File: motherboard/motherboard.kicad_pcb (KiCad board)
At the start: 2 copper layers, 79.8 x 53.3 mm, 54 parts, among them J1 locked, J2 PROGRAM, J3 Battery / Pitot/ Orientation, J4 c02 censor, J5 shaftencorder, J6 USB_C_Receptacle_USB2.0, J7 SparLoad, J8 lidar, J9 Control Board, Q1 2N7002K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

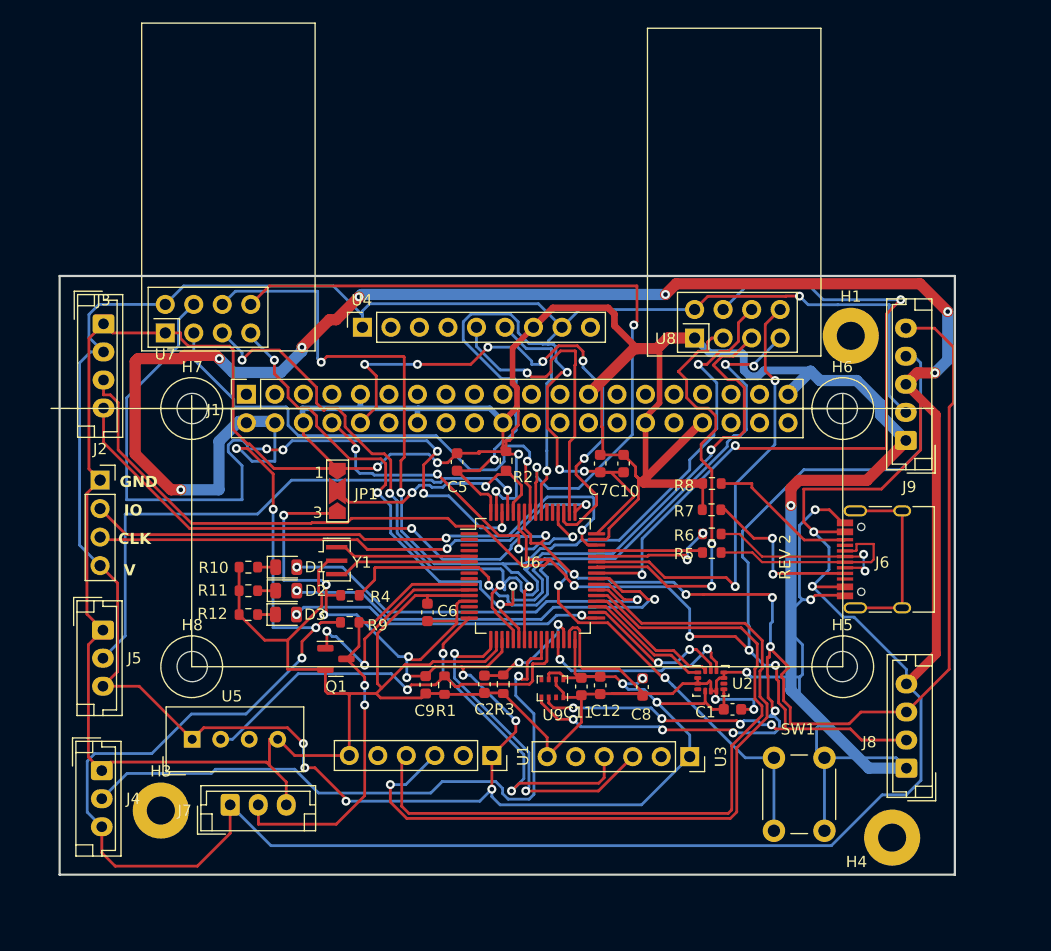
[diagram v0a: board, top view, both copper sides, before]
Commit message: PCB Rev2 Layout
PCB layout revised with ground and power pours, differential routing for USB, fixes for USB and programming pins. Passes DRC.
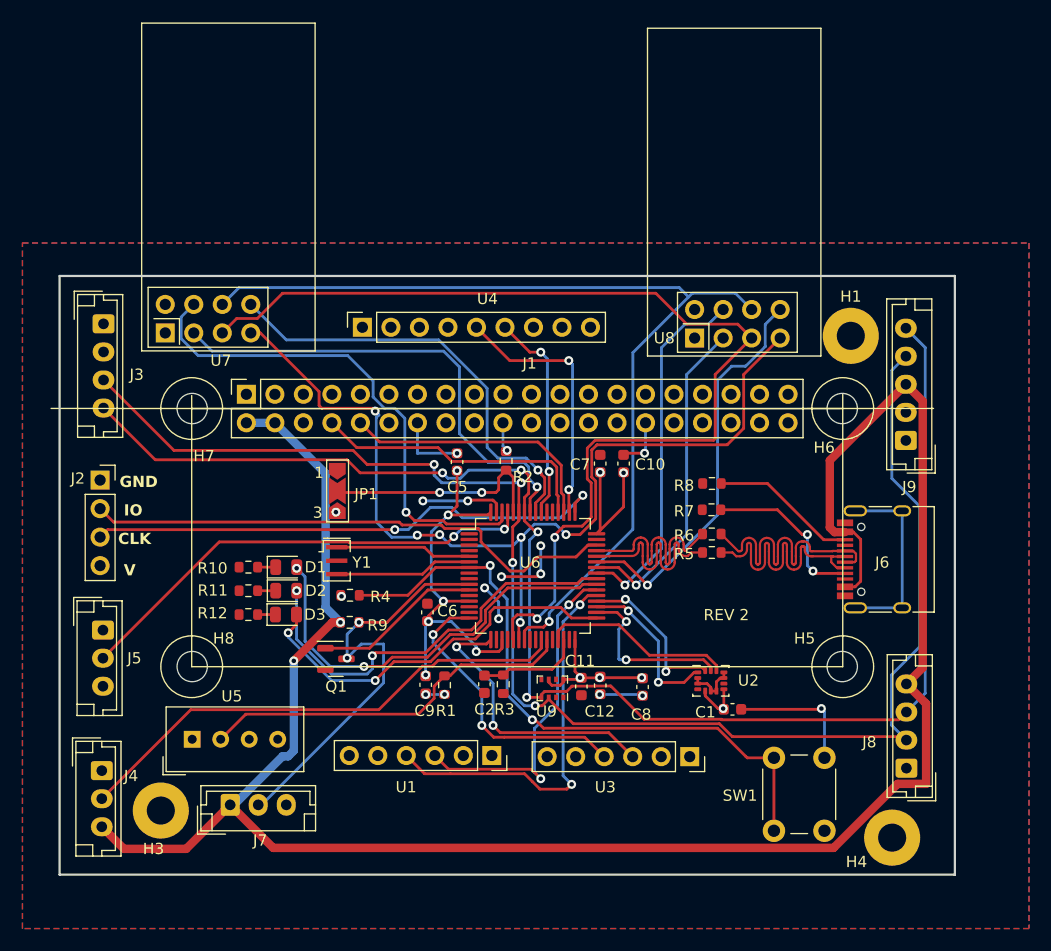
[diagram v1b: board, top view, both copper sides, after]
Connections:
- net Net-(D1-A) renamed /LED1
- net Net-(D2-A) renamed /LED2
- net Net-(D3-A) renamed /LED3
- R5 pad 1: /USB_{D+} -> /USB-
- R5 pad 2: /D+ -> /D-
- R6 pad 1: /USB_{D-} -> /USB+
- R6 pad 2: /D- -> /D+
- U6 pad 44: /USB_{D-} -> /USB-
- U6 pad 45: /USB_{D+} -> /USB+
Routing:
- net GND: track 500.0 -> 52.7 mm, vias 10 -> 15
- net +3.3V: track 352.2 -> 65.7 mm, vias 19 -> 14
- net +5V: track 346.3 -> 185.5 mm, vias 13 -> 2
- net /USART6_{RX}: track 71.7 -> 30.3 mm, vias 1 -> 2
- net /I2C_{SCK}: track 170.0 -> 133.5 mm, vias 10 -> 4
- net /USART6_{TX}: track 66.8 -> 35.0 mm, vias 0 -> 2
- net /TELE_{CS}-E: track 63.8 -> 32.4 mm, vias 3 -> 1
- net /I2C_{SDA}: track 161.6 -> 135.4 mm, vias 8 -> 4
- net /TELE_{IRQ}-int: track 64.3 -> 39.1 mm, vias 2 -> 1
- net /USART3_{TX}: track 49.0 -> 23.7 mm, vias 6 -> 0
- net /TELE_{CS}-int: track 69.6 -> 45.5 mm, vias 5 -> 1
- net /USB+: track 0.00 -> 19.8 mm
- net /USB-: track 0.00 -> 19.3 mm
- net /CO_{2}: track 58.8 -> 45.5 mm, vias 1 -> 0
- net /USB_{D-}: track 11.5 -> 0.00 mm, vias 2 -> 0
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- added copper zone on B.Cu, net +3.3V
- added copper zone on F.Cu, net GND
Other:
- board text added: "Ethan Todd"

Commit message: Touched up layout
Updated title block and made revision label used title block value
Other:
- board text added: "REV ${REVISION}"
- board text removed: "REV 2"
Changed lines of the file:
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@@
   (paper "A4")
   (title_block
-    (rev "REV2")
+    (title "Falcon Motherboard")
+    (date "2024-02-15")
+    (rev "2")
+    (company "HPVDT")
   )
   (layers
@@
     (effects (font (size 1 1) (thickness 0.25) bold) (justify left bottom))
   )
-  (gr_text "REV 2" (at 129.5 91.75) (layer "F.SilkS" knockout)
+  (gr_text "REV ${REVISION}" (at 129.5 91.75) (layer "F.SilkS" knockout)
     (effects (font (size 1 1) (thickness 0.15)) (justify left bottom))
   )

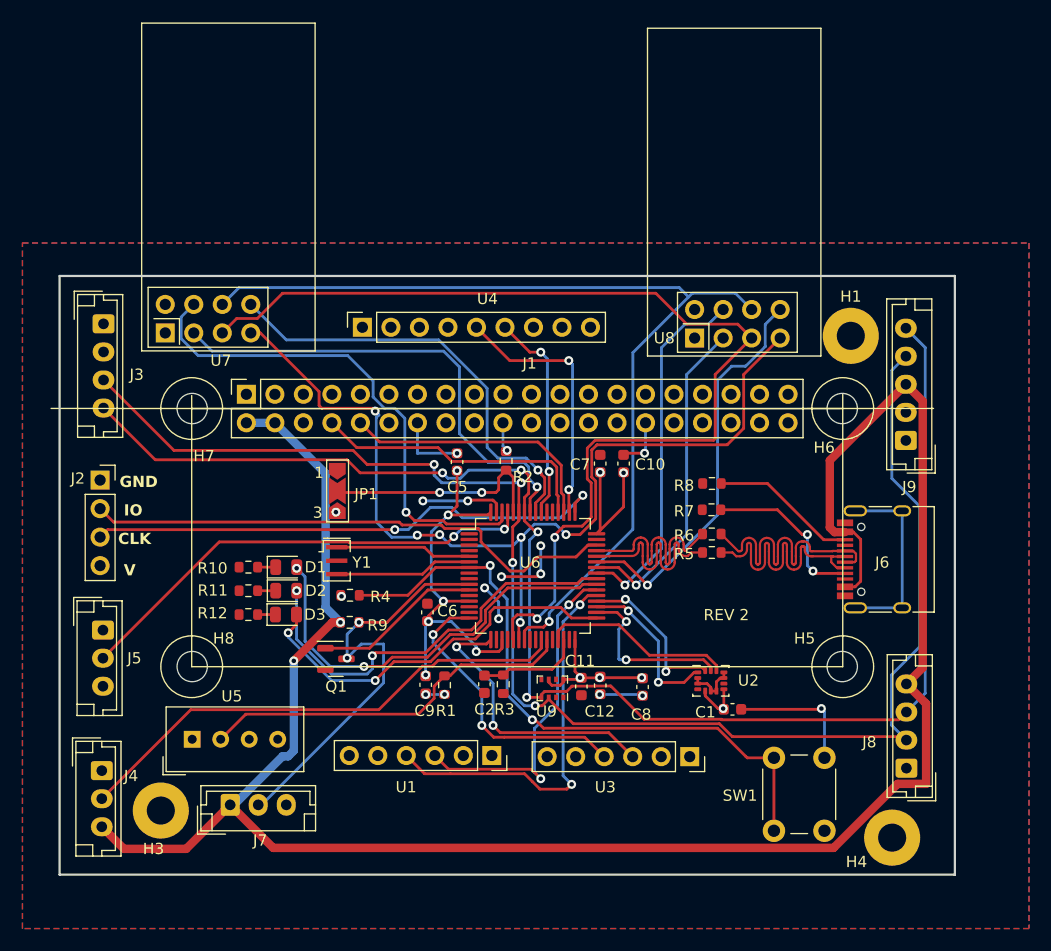
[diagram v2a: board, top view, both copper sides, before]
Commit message: Added extra LEDs, replaced Voltage reg., added redundant SW, reviewed USB placement
Added many new features
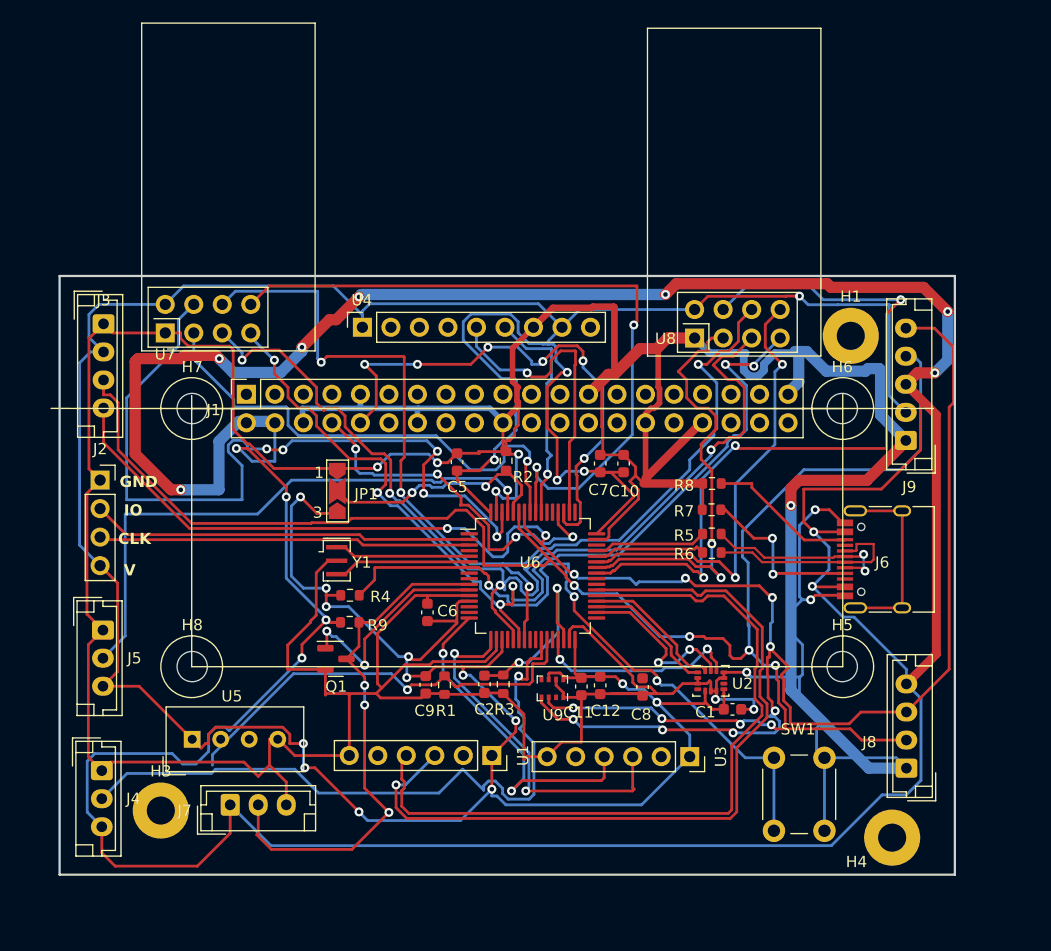
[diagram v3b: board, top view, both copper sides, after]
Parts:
- removed D1, D2, D3: LED, LED_SMD:LED_0805_2012Metric
- removed R10, R11, R12: 130R, Resistor_SMD:R_0603_1608Metric
- renumbered R6 to R5, R5 to R6
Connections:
- net /USB+ renamed /USB_{D-}
- net /USB- renamed /USB_{D+}
- R5 pad 2: /D+ -> /D-
- R6 pad 2: /D- -> /D+
- U6 pad 2: unconnected-(U6-PC13-Pad2) -> /SWDIO
- U6 pad 3: unconnected-(U6-PC14-Pad3) -> /SWCLK
- U6 pad 33: /LED3 -> unconnected-(U6-PB12-Pad33)
- U6 pad 39: /LED1 -> unconnected-(U6-PC8-Pad39)
- U6 pad 40: /LED2 -> unconnected-(U6-PC9-Pad40)
- U6 pad 46: /SWDIO -> unconnected-(U6-PA13-Pad46)
- U6 pad 49: /SWCLK -> unconnected-(U6-PA14-Pad49)
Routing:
- net GND: track 52.7 -> 498.5 mm, vias 15 -> 10
- net +3.3V: track 65.7 -> 353.4 mm, vias 14 -> 18
- net +5V: track 185.5 -> 346.9 mm, vias 2 -> 13
- net /USART6_{RX}: track 30.3 -> 72.0 mm, vias 2 -> 1
- net /I2C_{SCK}: track 133.5 -> 171.2 mm, vias 4 -> 10
- net /LED1: track 37.5 -> 0.00 mm, vias 2 -> 0
- net /LED2: track 37.2 -> 0.00 mm, vias 2 -> 0
- net /TELE_{CS}-E: track 32.4 -> 68.2 mm, vias 1 -> 3
- net /LED3: track 35.1 -> 0.00 mm, vias 2 -> 0
- net /USART6_{TX}: track 35.0 -> 68.1 mm, vias 2 -> 0
- net /I2C_{SDA}: track 135.4 -> 162.7 mm, vias 4 -> 8
- net /TELE_{CS}-int: track 45.5 -> 70.9 mm, vias 1 -> 5
- net /TELE_{IRQ}-int: track 39.1 -> 64.3 mm, vias 1 -> 2
- net /USART3_{TX}: track 23.7 -> 47.8 mm, vias 0 -> 6
- net /CO_{2}: track 45.5 -> 61.0 mm, vias 0 -> 1
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- removed copper zone on B.Cu, net +3.3V
- removed copper zone on F.Cu, net GND
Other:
- board text removed: "Ethan Todd"
- board text removed: "REV ${REVISION}"

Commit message: Final touches
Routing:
- net /DHT22: track 39.1 -> 36.8 mm
- net /CO_{2}: track 61.0 -> 58.8 mm
- net +5V: track 346.9 -> 344.9 mm
- net /USART2_{RX}: track 32.2 -> 30.4 mm
- net GND: track 498.5 -> 496.9 mm
- net /I2C_{SDA}: track 162.7 -> 161.6 mm
- net unconnected-(J1-3V3-Pad17): track 0.69 -> 0.00 mm
- net +3.3V: track 353.4 -> 353.7 mm, vias 18 -> 19
- net /OneWire_{RX}: vias 3 -> 2

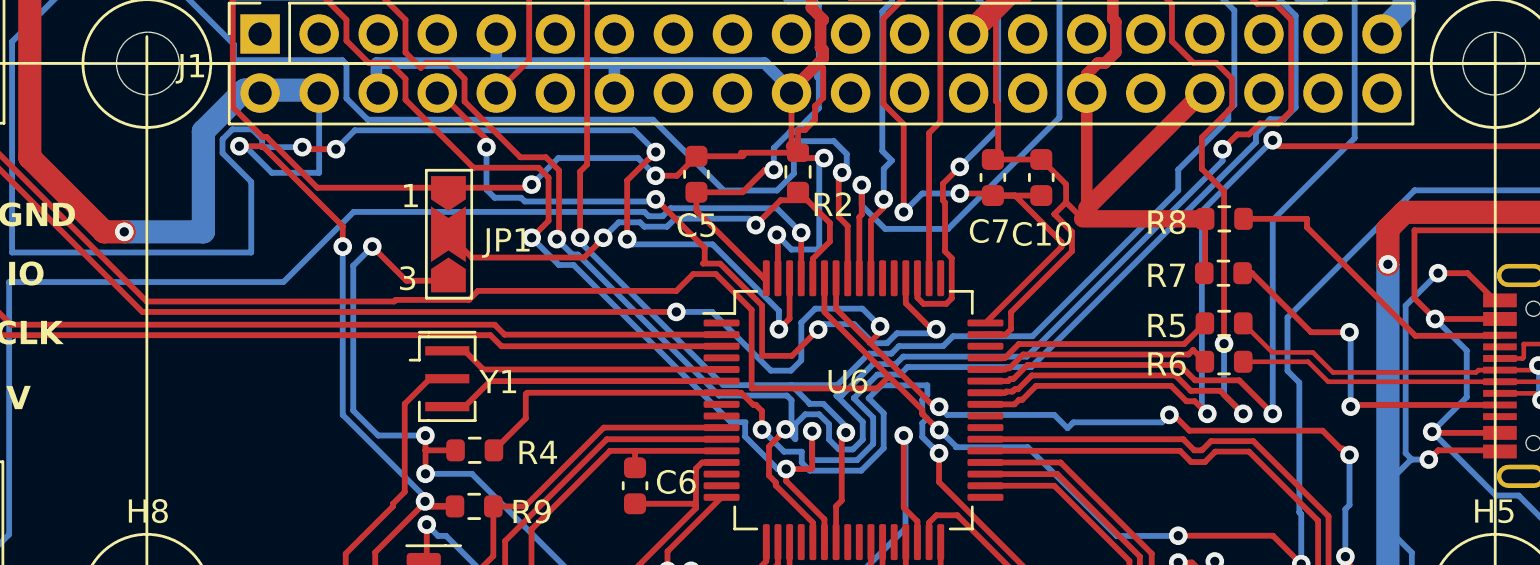
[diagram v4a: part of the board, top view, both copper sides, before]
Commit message: Revised Motherboard design with correct programming pin connections
Changed schematic with correct pins for programming and updated board to reflect this. Moved some traces to fit the new traces in.
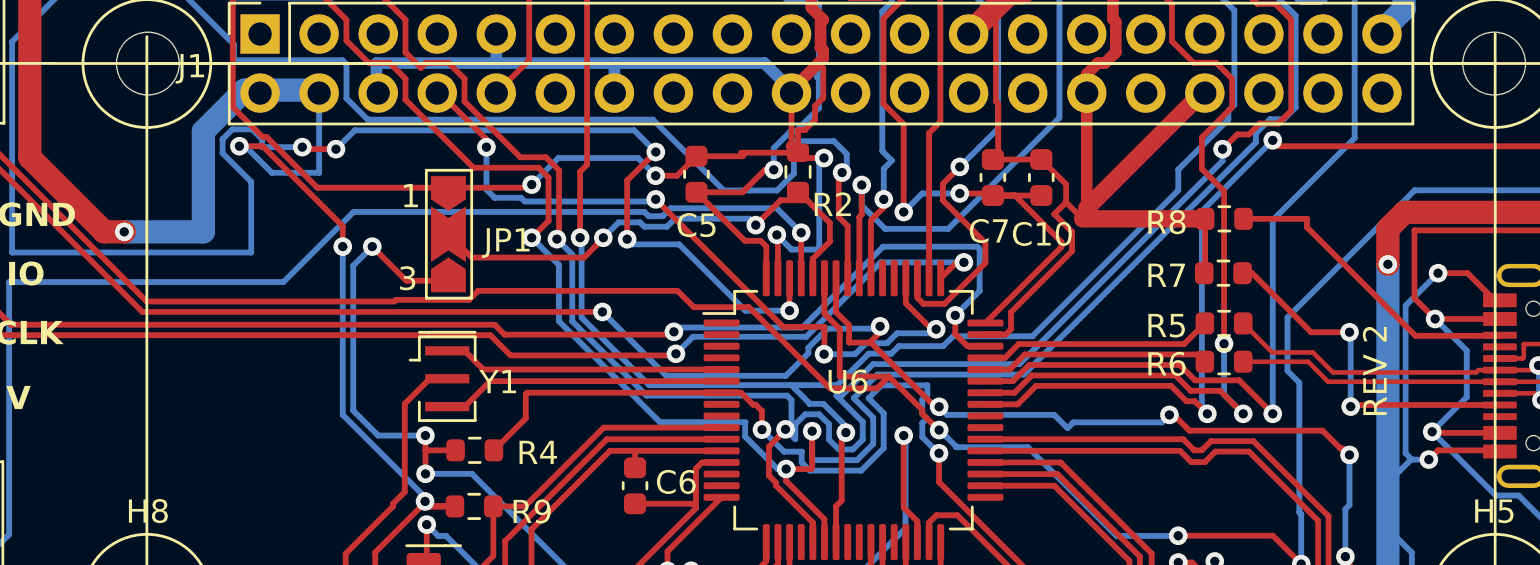
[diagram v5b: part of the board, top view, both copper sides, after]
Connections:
- U6 pad 2: /SWDIO -> unconnected-(U6-PC13-Pad2)
- U6 pad 3: /SWCLK -> unconnected-(U6-PC14-Pad3)
- U6 pad 46: unconnected-(U6-PA13-Pad46) -> /SWDIO
- U6 pad 49: unconnected-(U6-PA14-Pad49) -> /SWCLK
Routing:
- net /SWDIO: track 34.0 -> 52.3 mm, vias 0 -> 2
- net /SWCLK: track 33.2 -> 46.7 mm, vias 0 -> 2
- net /SPI1MOSI: track 94.3 -> 96.1 mm
- net /USART3_{RX}: track 33.3 -> 31.5 mm
- net /SPI1SCK: track 90.4 -> 92.0 mm
- net /SPI1MISO: track 87.2 -> 88.6 mm
- net /I2C_{SDA}: track 161.6 -> 160.2 mm
- net /TELE_{CS}-int: track 70.9 -> 69.6 mm
- net /USART3_{TX}: track 47.8 -> 49.0 mm
- net /I2C_{SCK}: track 171.2 -> 170.5 mm
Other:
- board text added: "REV 2"

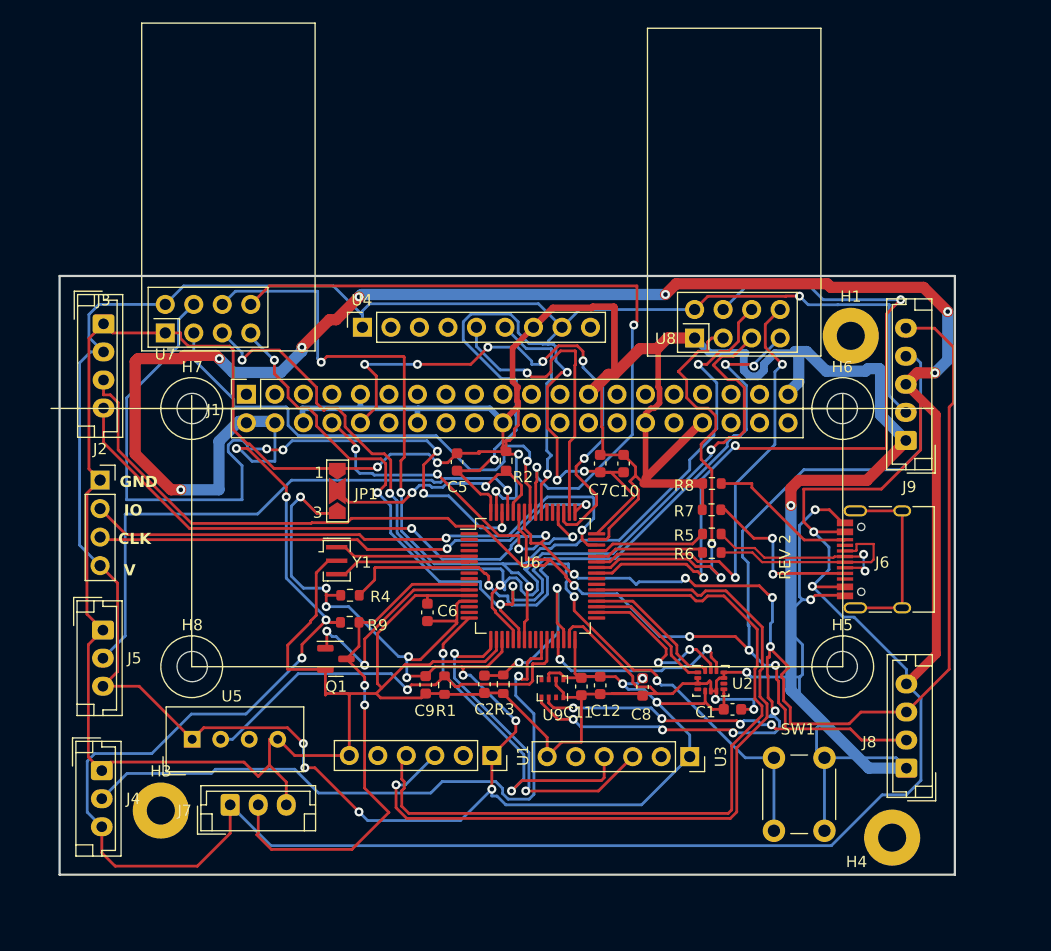
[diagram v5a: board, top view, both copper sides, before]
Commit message: Status leds
Added 3 status LEDs and resistors on the left side of the board. Moved some traces and vias but left all components locked in position.
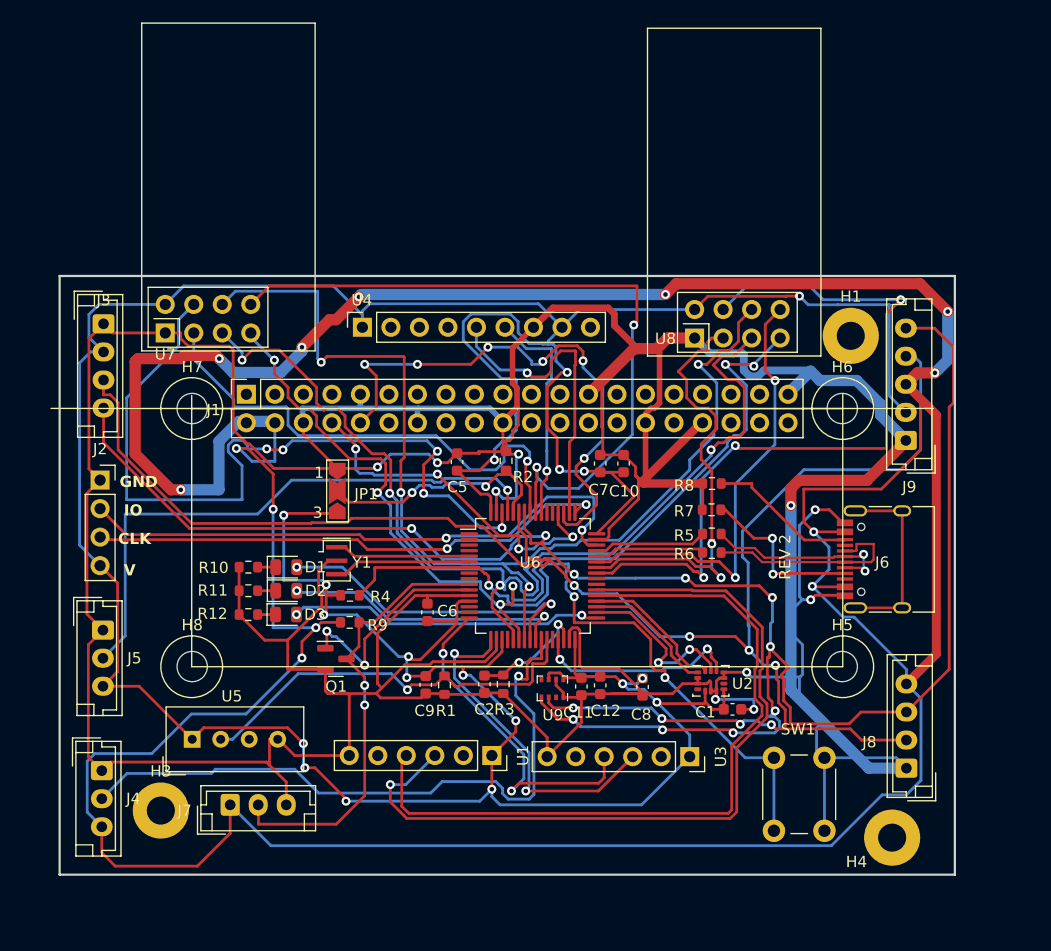
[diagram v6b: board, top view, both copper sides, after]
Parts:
- added D1: LED, LED_SMD:LED_0805_2012Metric, F.Cu at (92.3, 86.9)
- added D2: LED, LED_SMD:LED_0805_2012Metric, F.Cu at (92.3, 89.0)
- added D3: LED, LED_SMD:LED_0805_2012Metric, F.Cu at (92.3, 91.1)
- added R10: 130R, Resistor_SMD:R_0603_1608Metric, F.Cu at (89.0, 86.9)
- added R11: 130R, Resistor_SMD:R_0603_1608Metric, F.Cu at (89.0, 89.0)
- added R12: 130R, Resistor_SMD:R_0603_1608Metric, F.Cu at (89.0, 91.1)
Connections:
- U6 pad 24: unconnected-(U6-PC4-Pad24) -> Net-(D1-A)
- U6 pad 25: unconnected-(U6-PC5-Pad25) -> Net-(D2-A)
- U6 pad 33: unconnected-(U6-PB12-Pad33) -> Net-(D3-A)
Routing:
- net Net-(D1-A): track 0.00 -> 28.8 mm, vias 0 -> 2
- net Net-(D3-A): track 0.00 -> 28.0 mm, vias 0 -> 2
- net Net-(D2-A): track 0.00 -> 25.6 mm, vias 0 -> 2
- net /OneWire_{RX}: track 46.6 -> 40.0 mm
- net Net-(U6-VCAP_1): track 17.0 -> 10.5 mm
- net GND: track 496.9 -> 500.2 mm
- net /RST: track 60.8 -> 62.9 mm
- net +3.3V: track 354.1 -> 352.2 mm
- net Net-(D2-K): track 0.00 -> 1.61 mm
- net Net-(D1-K): track 0.00 -> 1.61 mm
- net Net-(D3-K): track 0.00 -> 1.59 mm
- net +5V: track 344.9 -> 346.3 mm
- net /USART6_{TX}: track 68.1 -> 67.6 mm
- net /TELE_{IRQ}-E: track 40.3 -> 39.8 mm
